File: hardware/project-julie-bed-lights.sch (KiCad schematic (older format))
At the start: 11 parts, among them J1 2199230-4

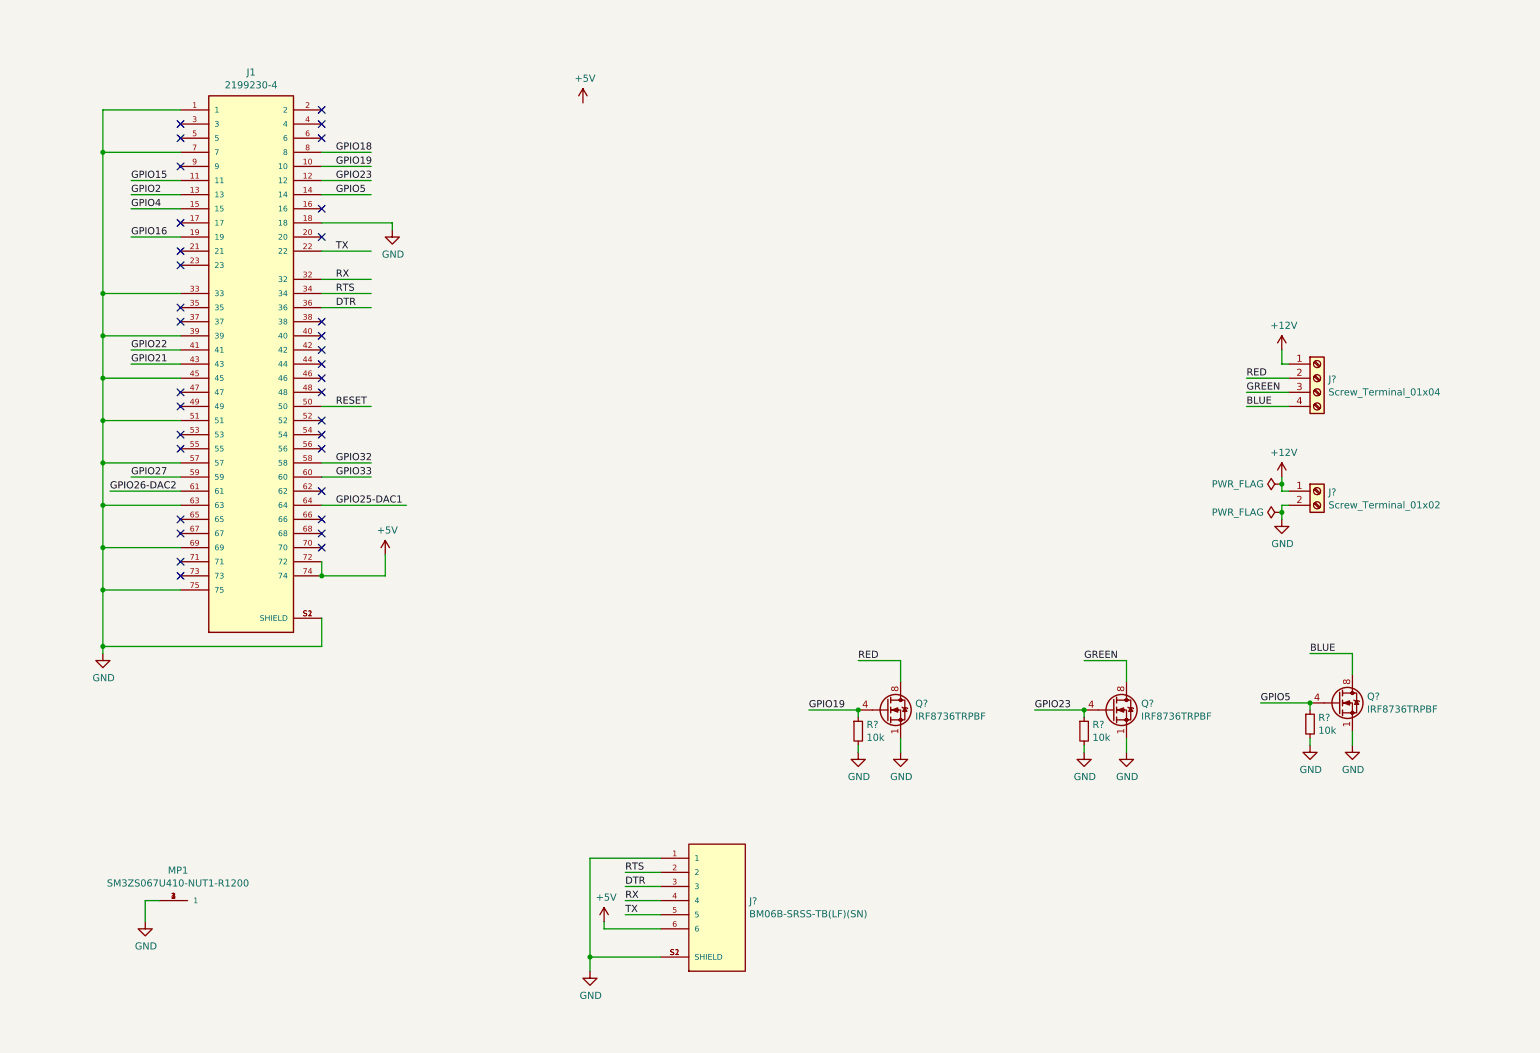
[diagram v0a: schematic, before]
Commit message: Added DC-DC converter
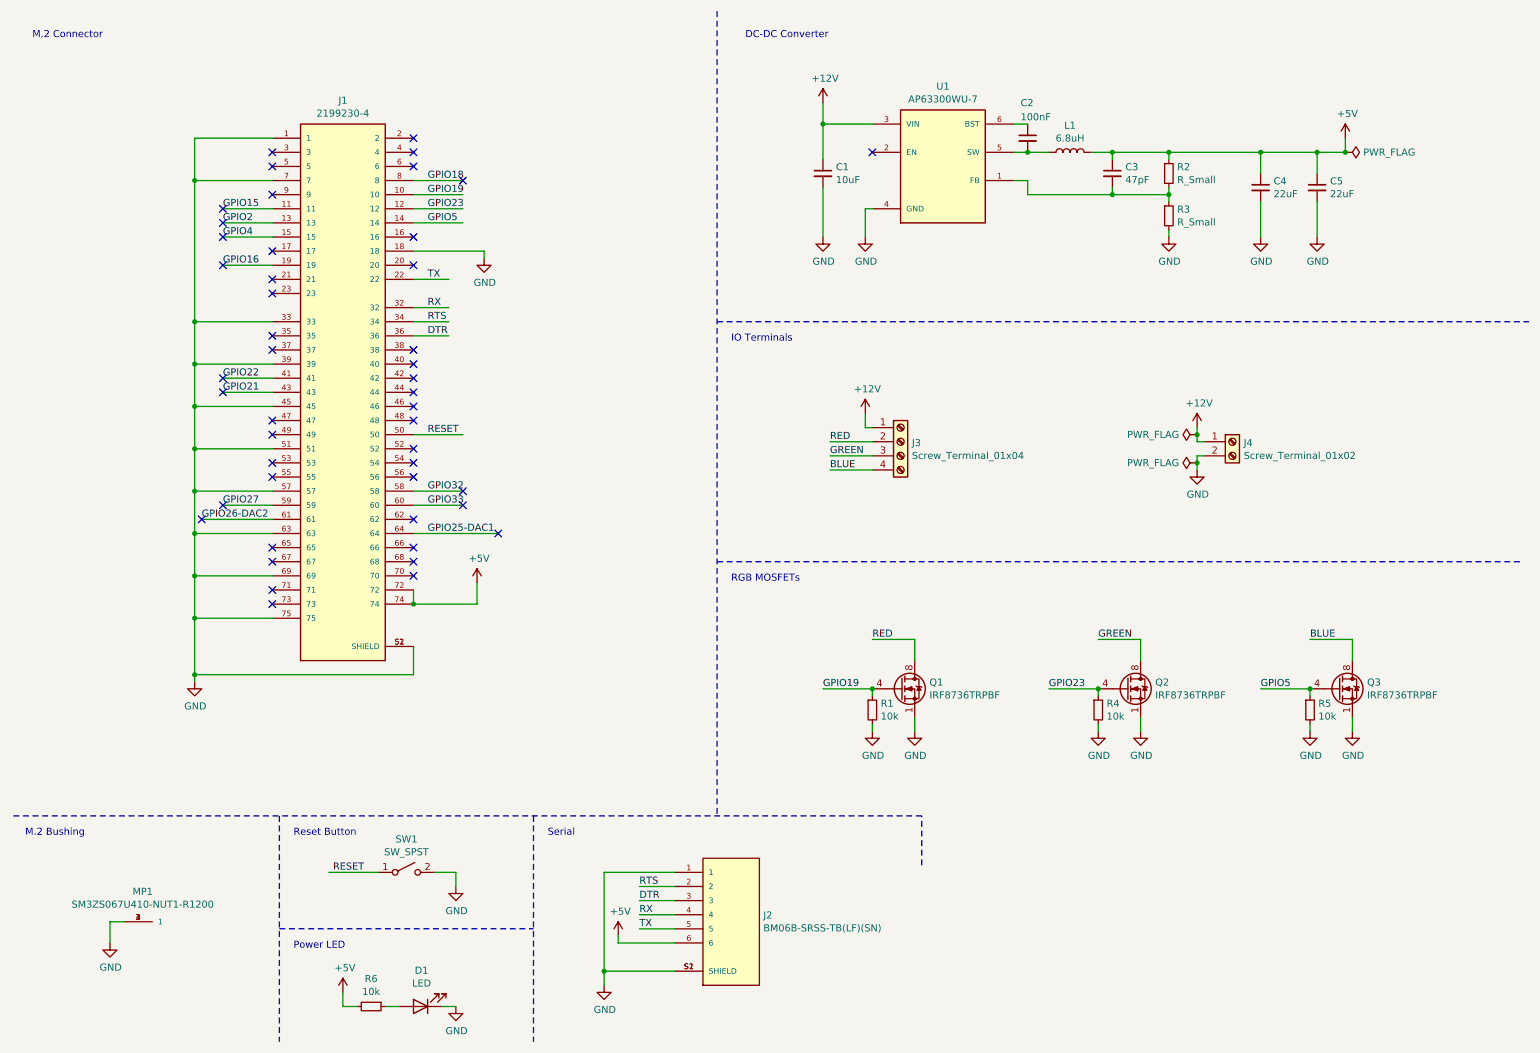
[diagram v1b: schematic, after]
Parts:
- added C1: 10uF, Capacitor_SMD:C_1210_3225Metric_Pad1.33x2.70mm_HandSolder, symbol Device:C_Small
- added C2: 100nF, Capacitor_SMD:C_0603_1608Metric, symbol Device:C_Small
- added C3: 47pF, Capacitor_SMD:C_0603_1608Metric, symbol Device:C_Small
- added C4, C5: 22uF, Capacitor_SMD:C_1210_3225Metric_Pad1.33x2.70mm_HandSolder, symbol Device:C_Small
- added D1: LED, symbol Device:LED
- added L1: 6.8uH, SRP4020TA-6R8M:IND_SRP4020TA-6R8M, symbol Device:L
- added R2, R3: R_Small, Resistor_SMD:R_0603_1608Metric, symbol Device:R_Small
- added R6: 10k, Resistor_SMD:R_0603_1608Metric, symbol Device:R_Small
- added SW1: SW_SPST, Button_Switch_SMD:SW_SPST_B3U-1000P, symbol Switch:SW_SPST
- added U1: AP63300WU-7, SOT95P280X100-6N, symbol AP63300WU-7:AP63300WU-7
- gave numbers to parts that had none: 9
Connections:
- wire segments 89 -> 125
- no-connect marks 34 -> 47
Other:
- note added: "DC-DC Converter"
- note added: "IO Terminals"
- note added: "M.2 Bushing"
- note added: "M.2 Connector"
- note added: "Power LED"
- note added: "RGB MOSFETs"
- note added: "Reset Button"
- note added: "Serial"
- moved on the sheet: J1, J2, J3, J4, MP1, Q1, Q2, Q3, R1, R4, R5

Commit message: First placement
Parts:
- D1: footprint (none) -> LED_SMD:LED_0603_1608Metric
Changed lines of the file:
@@
 Text Label 6300 3650 0    50   ~ 0
 GREEN
-Wire Wire Line
-	6600 3750 6300 3750
 Text Label 6300 3750 0    50   ~ 0
 BLUE
@@
 	1    0    0    -1
 $EndComp
-$Comp
-L Device:C_Small C3
-U 1 1 6044F01A
-P 8300 1650
-F 0 "C3" H 8392 1696 50  0000 L CNN
-F 1 "47pF" H 8392 1605 50  0000 L CNN
-F 2 "Capacitor_SMD:C_0603_1608Metric" H 8300 1650 50  0001 C CNN
-F 3 "~" H 8300 1650 50  0001 C CNN
-	1    8300 1650
-	1    0    0    -1
-$EndComp
 NoConn ~ 6600 1500
 Wire Wire Line
@@
 	1    0    0    -1
 $EndComp
-$Comp
-L Device:C_Small C2
-U 1 1 604781F0
-P 7700 1400
-F 0 "C2" H 7650 1650 50  0000 L CNN
-F 1 "100nF" H 7650 1550 50  0000 L CNN
-F 2 "Capacitor_SMD:C_0603_1608Metric" H 7700 1400 50  0001 C CNN
-F 3 "~" H 7700 1400 50  0001 C CNN
-	1    7700 1400
-	1    0    0    -1
-$EndComp
 Wire Wire Line
 	7600 1300 7700 1300
@@
 	6250 1150 6250 1300
 Connection ~ 6250 1300
-$Comp
-L Device:L L1
-U 1 1 6049A68E
-P 8000 1500
-F 0 "L1" V 8190 1500 50  0000 C CNN
-F 1 "6.8uH" V 8099 1500 50  0000 C CNN
-F 2 "SRP4020TA-6R8M:IND_SRP4020TA-6R8M" H 8000 1500 50  0001 C CNN
-F 3 "~" H 8000 1500 50  0001 C CNN
-	1    8000 1500
-	0    -1   -1   0
-$EndComp
-Wire Wire Line
-	7700 1500 7850 1500
-Connection ~ 7700 1500
 $Comp
 L power:GND #PWR0120
@@
 	9750 1850 9750 2100
 Wire Wire Line
-	8150 1500 8300 1500
-Wire Wire Line
 	8300 1500 8300 1550
 Wire Wire Line
@@
 	8700 1500 8300 1500
 Connection ~ 8700 1500
-Connection ~ 8300 1500
 Wire Wire Line
 	8700 1750 8700 1800
@@
 F 0 "D1" H 3393 7295 50  0000 C CNN
 F 1 "LED" H 3393 7386 50  0000 C CNN
-F 2 "" H 3400 7550 50  0001 C CNN
+F 2 "LED_SMD:LED_0603_1608Metric" H 3400 7550 50  0001 C CNN
 F 3 "~" H 3400 7550 50  0001 C CNN
 	1    3400 7550
@@
 Wire Wire Line
 	3600 2600 3350 2600
+Wire Wire Line
+	6300 3750 6600 3750
+Connection ~ 8300 1500
+Connection ~ 7700 1500
+Wire Wire Line
+	8150 1500 8300 1500
+Wire Wire Line
+	7700 1500 7850 1500
+$Comp
+L Device:L L1
+U 1 1 6049A68E
+P 8000 1500
+F 0 "L1" V 8190 1500 50  0000 C CNN
+F 1 "6.8uH" V 8099 1500 50  0000 C CNN
+F 2 "SRP4020TA-6R8M:IND_SRP4020TA-6R8M" H 8000 1500 50  0001 C CNN
+F 3 "~" H 8000 1500 50  0001 C CNN
+	1    8000 1500
+	0    -1   -1   0
+$EndComp
+$Comp
+L Device:C_Small C2
+U 1 1 604781F0
+P 7700 1400
+F 0 "C2" H 7650 1650 50  0000 L CNN
+F 1 "100nF" H 7650 1550 50  0000 L CNN
+F 2 "Capacitor_SMD:C_0603_1608Metric" H 7700 1400 50  0001 C CNN
+F 3 "~" H 7700 1400 50  0001 C CNN
+	1    7700 1400
+	1    0    0    -1
+$EndComp
+$Comp
+L Device:C_Small C3
+U 1 1 6044F01A
+P 8300 1650
+F 0 "C3" H 8392 1696 50  0000 L CNN
+F 1 "47pF" H 8392 1605 50  0000 L CNN
+F 2 "Capacitor_SMD:C_0603_1608Metric" H 8300 1650 50  0001 C CNN
+F 3 "~" H 8300 1650 50  0001 C CNN
+	1    8300 1650
+	1    0    0    -1
+$EndComp
 $EndSCHEMATC

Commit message: Setup assembly print
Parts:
- R2: value R_Small -> 158k
- R3: value R_Small -> 30.1k
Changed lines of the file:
@@
 P 8700 1650
 F 0 "R2" H 8759 1696 50  0000 L CNN
-F 1 "R_Small" H 8759 1605 50  0000 L CNN
+F 1 "158k" H 8759 1605 50  0000 L CNN
 F 2 "Resistor_SMD:R_0603_1608Metric" H 8700 1650 50  0001 C CNN
 F 3 "~" H 8700 1650 50  0001 C CNN
@@
 P 8700 1950
 F 0 "R3" H 8759 1996 50  0000 L CNN
-F 1 "R_Small" H 8759 1905 50  0000 L CNN
+F 1 "30.1k" H 8759 1905 50  0000 L CNN
 F 2 "Resistor_SMD:R_0603_1608Metric" H 8700 1950 50  0001 C CNN
 F 3 "~" H 8700 1950 50  0001 C CNN
